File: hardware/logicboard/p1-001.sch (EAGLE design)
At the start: 36 parts, among them J7 DIN5, K1A G5V1, K1B G5V1, K1C G5V1, T1A 2SC1815, T1B 2SC1815, T1C 2SC1815

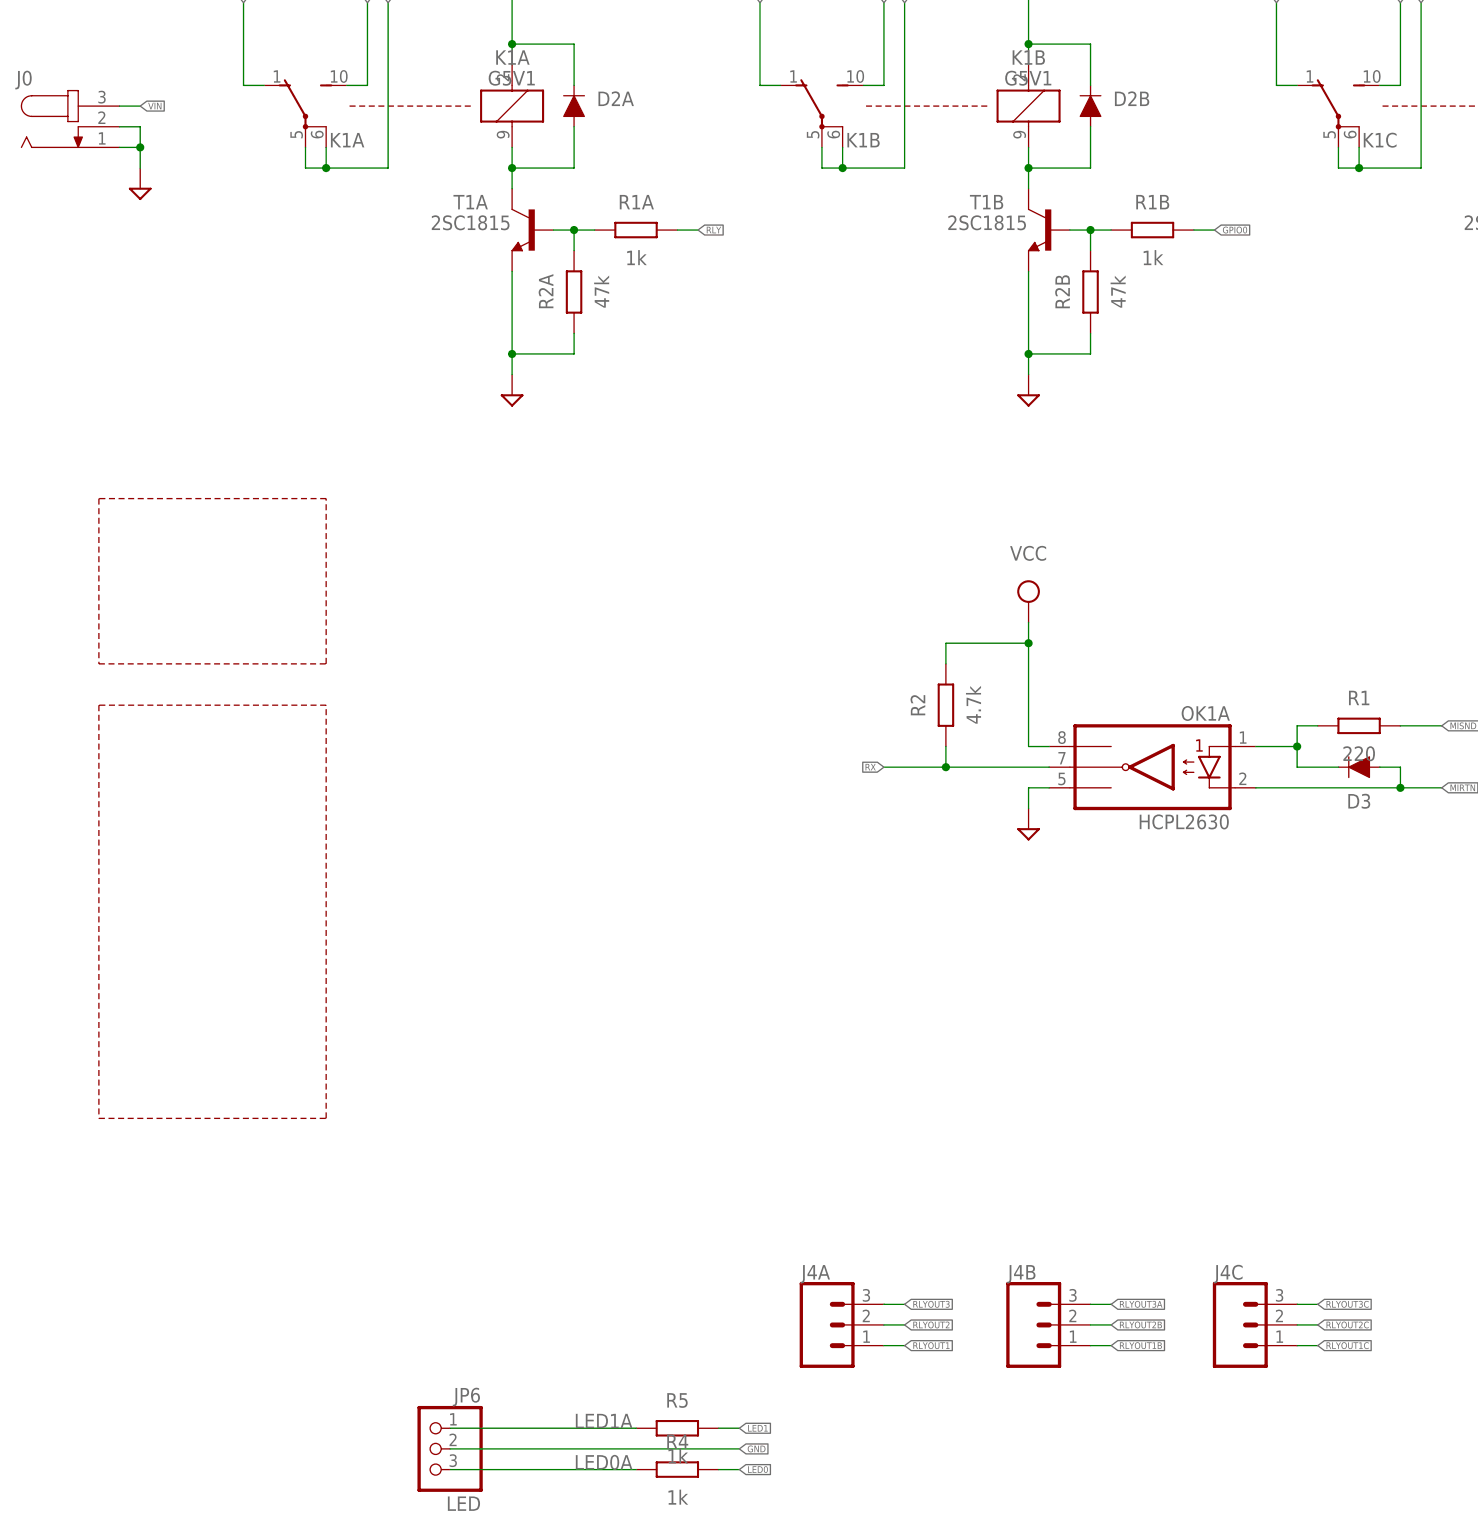
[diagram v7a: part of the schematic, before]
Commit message: Fixed signaling error.
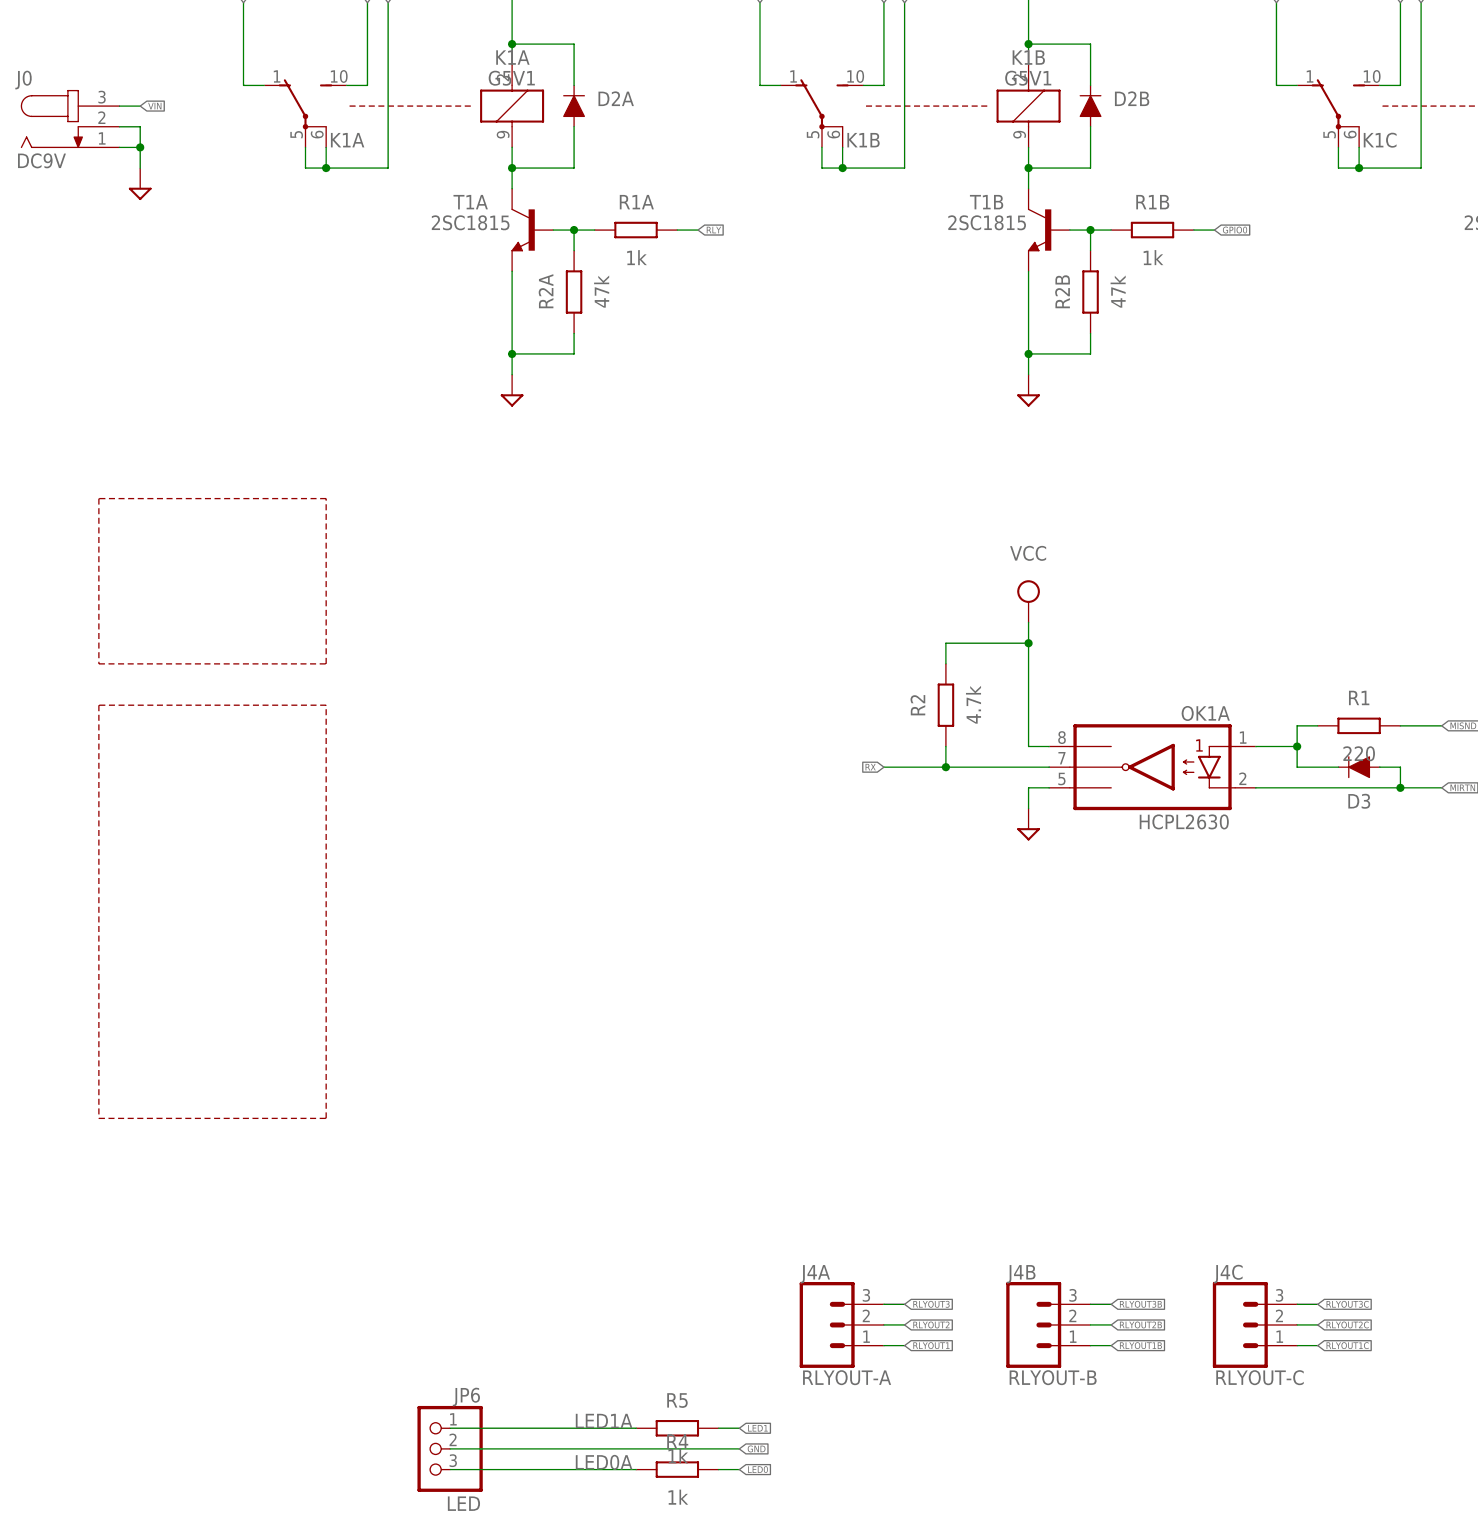
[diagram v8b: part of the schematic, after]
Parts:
- J0: value (none) -> DC9V
- J4A: value (none) -> RLYOUT-A
- J4B: value (none) -> RLYOUT-B
- J4C: value (none) -> RLYOUT-C
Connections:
- removed net RLYOUT3A: J4B.3
- net RLYOUT3B: now also J4B.3
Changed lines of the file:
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@@
 <part name="SUPPLY1" library="supply2" deviceset="GND" device=""/>
 <part name="J7" library="SparkFun-Connectors" library_urn="urn:adsk.eagle:library:513" deviceset="DIN5" device="" package3d_urn="urn:adsk.eagle:package:38294/1"/>
-<part name="J0" library="con-jack" library_urn="urn:adsk.eagle:library:154" deviceset="JACK-PLUG" device="0" package3d_urn="urn:adsk.eagle:package:7492/1"/>
+<part name="J0" library="con-jack" library_urn="urn:adsk.eagle:library:154" deviceset="JACK-PLUG" device="0" package3d_urn="urn:adsk.eagle:package:7492/1" value="DC9V"/>
 <part name="R4" library="resistor" library_urn="urn:adsk.eagle:library:348" deviceset="R-EU_" device="0204/5" package3d_urn="urn:adsk.eagle:package:23488/1" value="1k"/>
 <part name="R5" library="resistor" library_urn="urn:adsk.eagle:library:348" deviceset="R-EU_" device="0204/5" package3d_urn="urn:adsk.eagle:package:23488/1" value="1k"/>
@@
 <part name="SUPPLY9" library="supply2" library_urn="urn:adsk.eagle:library:372" deviceset="VCC" device=""/>
 <part name="SUPPLY10" library="supply2" library_urn="urn:adsk.eagle:library:372" deviceset="VCC" device=""/>
-<part name="J4A" library="SparkFun-Connectors" library_urn="urn:adsk.eagle:library:513" deviceset="CONN_03" device="JST-PTH" package3d_urn="urn:adsk.eagle:package:38069/1"/>
+<part name="J4A" library="SparkFun-Connectors" library_urn="urn:adsk.eagle:library:513" deviceset="CONN_03" device="JST-PTH" package3d_urn="urn:adsk.eagle:package:38069/1" value="RLYOUT-A"/>
 <part name="R1" library="resistor" library_urn="urn:adsk.eagle:library:348" deviceset="R-EU_" device="0204/5" package3d_urn="urn:adsk.eagle:package:23488/1" value="220"/>
 <part name="R2" library="resistor" library_urn="urn:adsk.eagle:library:348" deviceset="R-EU_" device="0204/5" package3d_urn="urn:adsk.eagle:package:23488/1" value="4.7k"/>
@@
 <part name="SUPPLY14" library="supply2" deviceset="GND" device=""/>
 <part name="SUPPLY15" library="supply2" library_urn="urn:adsk.eagle:library:372" deviceset="VCC" device=""/>
-<part name="J4B" library="SparkFun-Connectors" library_urn="urn:adsk.eagle:library:513" deviceset="CONN_03" device="JST-PTH" package3d_urn="urn:adsk.eagle:package:38069/1"/>
-<part name="J4C" library="SparkFun-Connectors" library_urn="urn:adsk.eagle:library:513" deviceset="CONN_03" device="JST-PTH" package3d_urn="urn:adsk.eagle:package:38069/1"/>
+<part name="J4B" library="SparkFun-Connectors" library_urn="urn:adsk.eagle:library:513" deviceset="CONN_03" device="JST-PTH" package3d_urn="urn:adsk.eagle:package:38069/1" value="RLYOUT-B"/>
+<part name="J4C" library="SparkFun-Connectors" library_urn="urn:adsk.eagle:library:513" deviceset="CONN_03" device="JST-PTH" package3d_urn="urn:adsk.eagle:package:38069/1" value="RLYOUT-C"/>
 </parts>
 <sheets>
@@
 </segment>
 </net>
-<net name="RLYOUT3A" class="0">
-<segment>
-<pinref part="J4B" gate="J$1" pin="3"/>
-<wire x1="144.78" y1="53.34" x2="147.32" y2="53.34" width="0.1524" layer="91"/>
-<label x="147.32" y="53.34" size="0.8128" layer="95" xref="yes"/>
-</segment>
-</net>
 <net name="RLYOUT1B" class="0">
 <segment>
@@
 <label x="104.14" y="213.36" size="0.8128" layer="95" rot="R90" xref="yes"/>
 </segment>
-</net>
+<segment>
+<pinref part="J4B" gate="J$1" pin="3"/>
+<wire x1="144.78" y1="53.34" x2="147.32" y2="53.34" width="0.1524" layer="91"/>
+<label x="147.32" y="53.34" size="0.8128" layer="95" xref="yes"/>
+</segment>
+</net>
